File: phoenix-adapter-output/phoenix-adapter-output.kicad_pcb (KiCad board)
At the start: 2 copper layers, 16.2 x 19 mm, 1 part, among them CON1 Headphone_Jack_2.5mm_SJ1-3523N

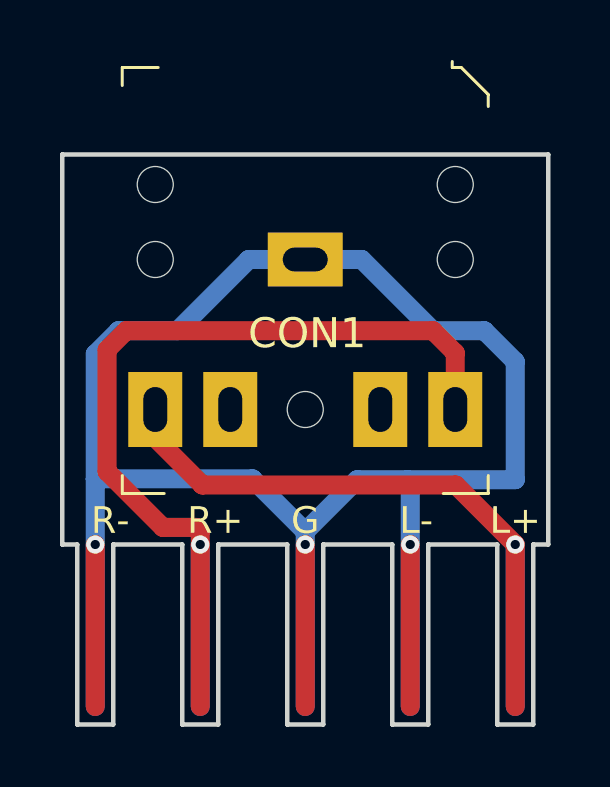
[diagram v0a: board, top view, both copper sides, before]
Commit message: Headphone Jack Version
Replaced stacked RCA jack with headphone jack (CUI SJ1-352XN or NG)
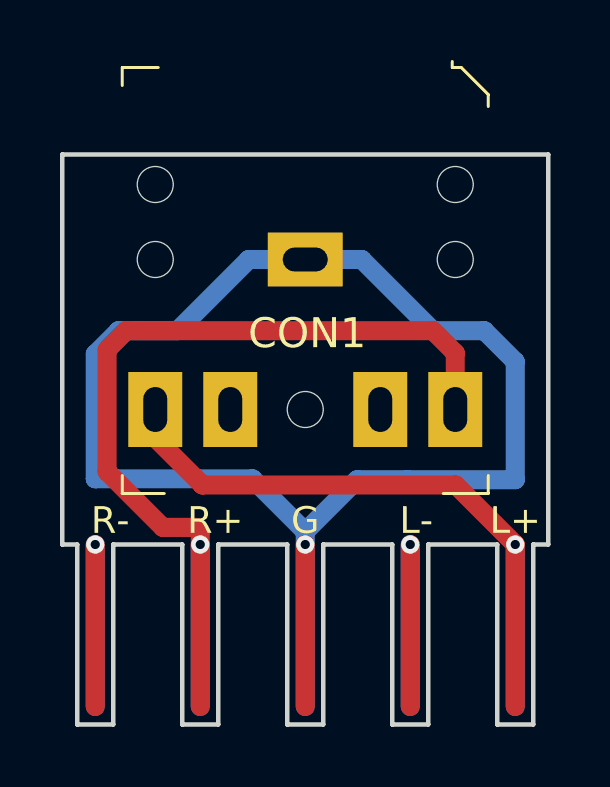
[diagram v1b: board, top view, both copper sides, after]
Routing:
- net (no net): track 135.8 -> 131.4 mm
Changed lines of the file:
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@@
     (thickness 1.6)
     (drawings 32)
-    (tracks 47)
+    (tracks 44)
     (zones 0)
     (modules 1)
@@
   (segment (start 141.427948 119.141) (end 139.7 120.868948) (width 0.635) (layer B.Cu) (net 0))
   (segment (start 146.7 115.204) (end 146.7 119.141) (width 0.635) (layer B.Cu) (net 0))
-  (segment (start 132.7 119.111) (end 132.7 121.3) (width 0.635) (layer B.Cu) (net 0))
-  (segment (start 143.2 119.227) (end 143.114 119.141) (width 0.635) (layer B.Cu) (net 0))
-  (segment (start 143.2 121.3) (end 143.2 119.227) (width 0.635) (layer B.Cu) (net 0))
   (segment (start 146.7 119.141) (end 143.114 119.141) (width 0.635) (layer B.Cu) (net 0))
   (segment (start 143.114 119.141) (end 141.427948 119.141) (width 0.635) (layer B.Cu) (net 0))

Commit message: Panels!
Added panels for 20 boards, either all one type or half and half. Untested so far, designed for jlcpcb
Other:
- board text added: "OUT"
- board text removed: "IN"
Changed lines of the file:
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@@
     )
   )
-  (gr_text IN (at 136.906 110.236) (layer B.SilkS)
+  (gr_text OUT (at 137.922 109.601) (layer B.SilkS)
     (effects (font (size 1.5 1.5) (thickness 0.3)) (justify mirror))
   )
